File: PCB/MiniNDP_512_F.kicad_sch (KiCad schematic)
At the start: 15 parts, among them J1 Conn_02x20_Odd_Even, U1 HC238, U2 HC4040, U3 FCT841, U4 AS6C4008, U5 2G00

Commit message: 512k F easy build
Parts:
- removed C5: 10u, 000_LOCAL:C_0805, symbol 000_LOCAL:C
- removed D1: BAS70-05, 000_LOCAL:SOT-23, symbol 000_LOCAL:BAV70
- removed R3: 47k, 000_LOCAL:R_0805, symbol 000_LOCAL:R
- added C1: 4.7u, 000_LOCAL:C_1206, symbol 000_LOCAL:C
- added D1, D2: LL4148, 000_LOCAL:D_MiniMELF, symbol 000_LOCAL:LL4148
- added R1: 47k, 000_LOCAL:R_1206, symbol 000_LOCAL:R
- C2: footprint 000_LOCAL:C_0805 -> 000_LOCAL:C_1206; MPN CL21B105KAFNNNE -> CL31B475KAHNNNE
- C3, C4: value 1u -> 4.7u; footprint 000_LOCAL:C_0805 -> 000_LOCAL:C_1206; MPN CL21B105KAFNNNE -> CL31B475KAHNNNE
- R2: footprint 000_LOCAL:R_0805 -> 000_LOCAL:R_1206; MPN RMCF0805FT47K0 -> CRGCQ1206F47K
- U1: MPN (none) -> 74HCT238D,653
- U2: MPN IC BINARY COUNTER 12-BIT 16SO -> 74HC4040D,653
- U3: MPN (none) -> CY74FCT841CTSOC
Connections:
- net +BATT: now also D2.2 (A)
- net GND: now also C1.2
- net RAMRST: now also R1.2; no longer R2.2
- net VBUS: now also C1.1, D1.2 (A); no longer C4.1
- net VMEM: now also C4.1, D1.1 (K), D2.1 (K), R1.1
- net ~{WR}: now also R2.2
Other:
- moved on the sheet: BT1

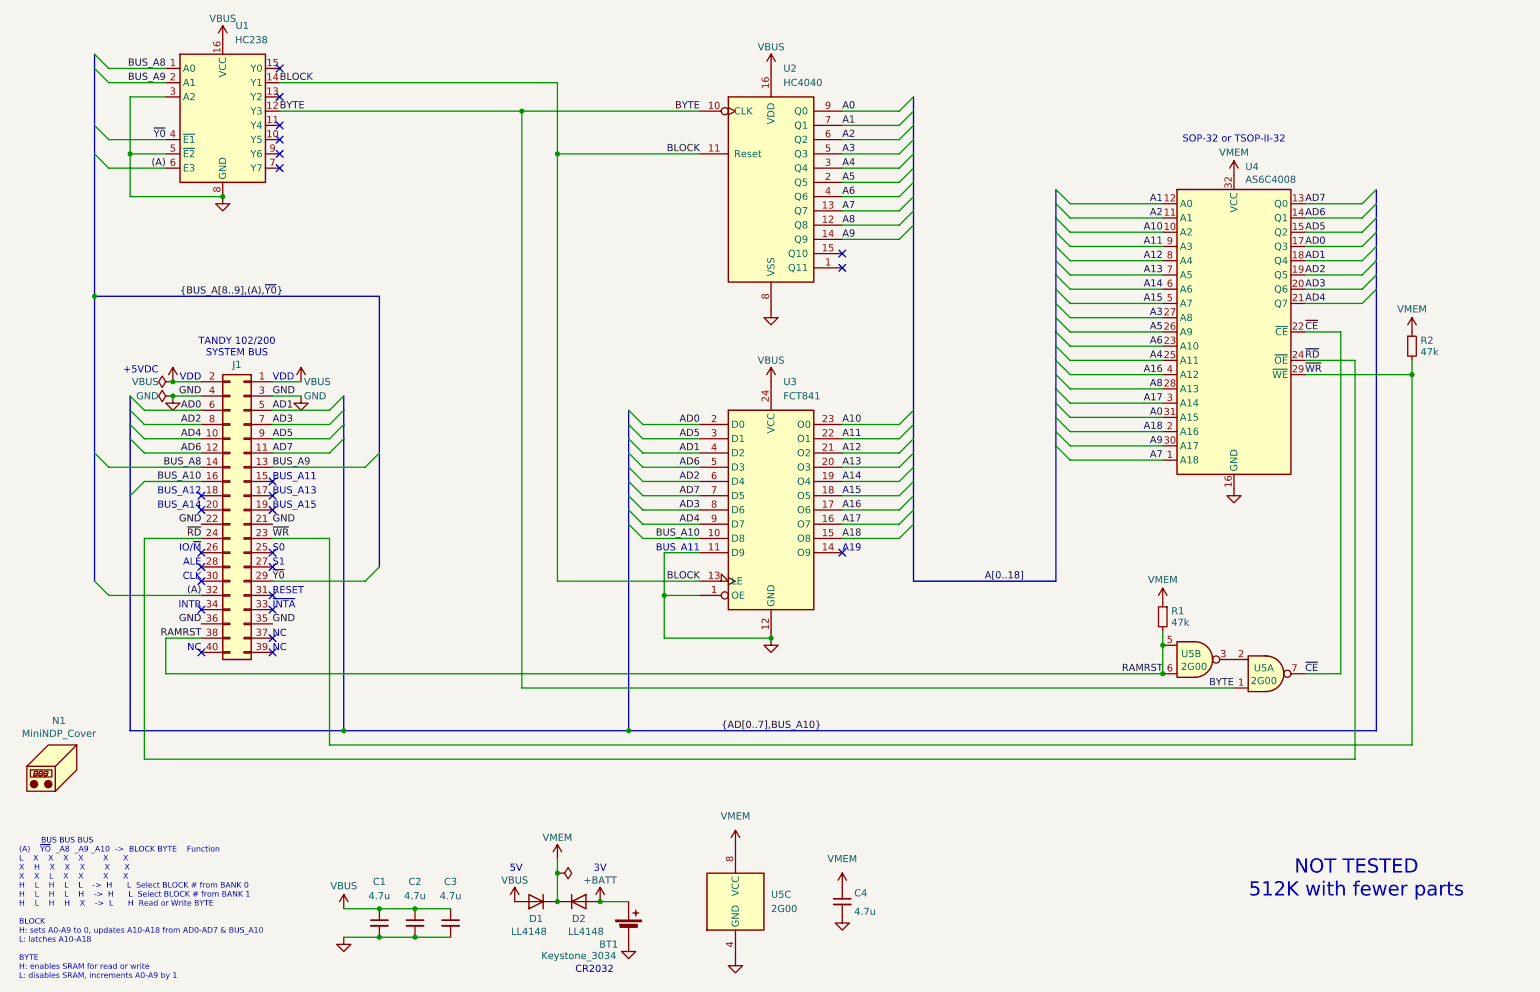
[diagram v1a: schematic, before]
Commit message: replace 512_F with 512_G
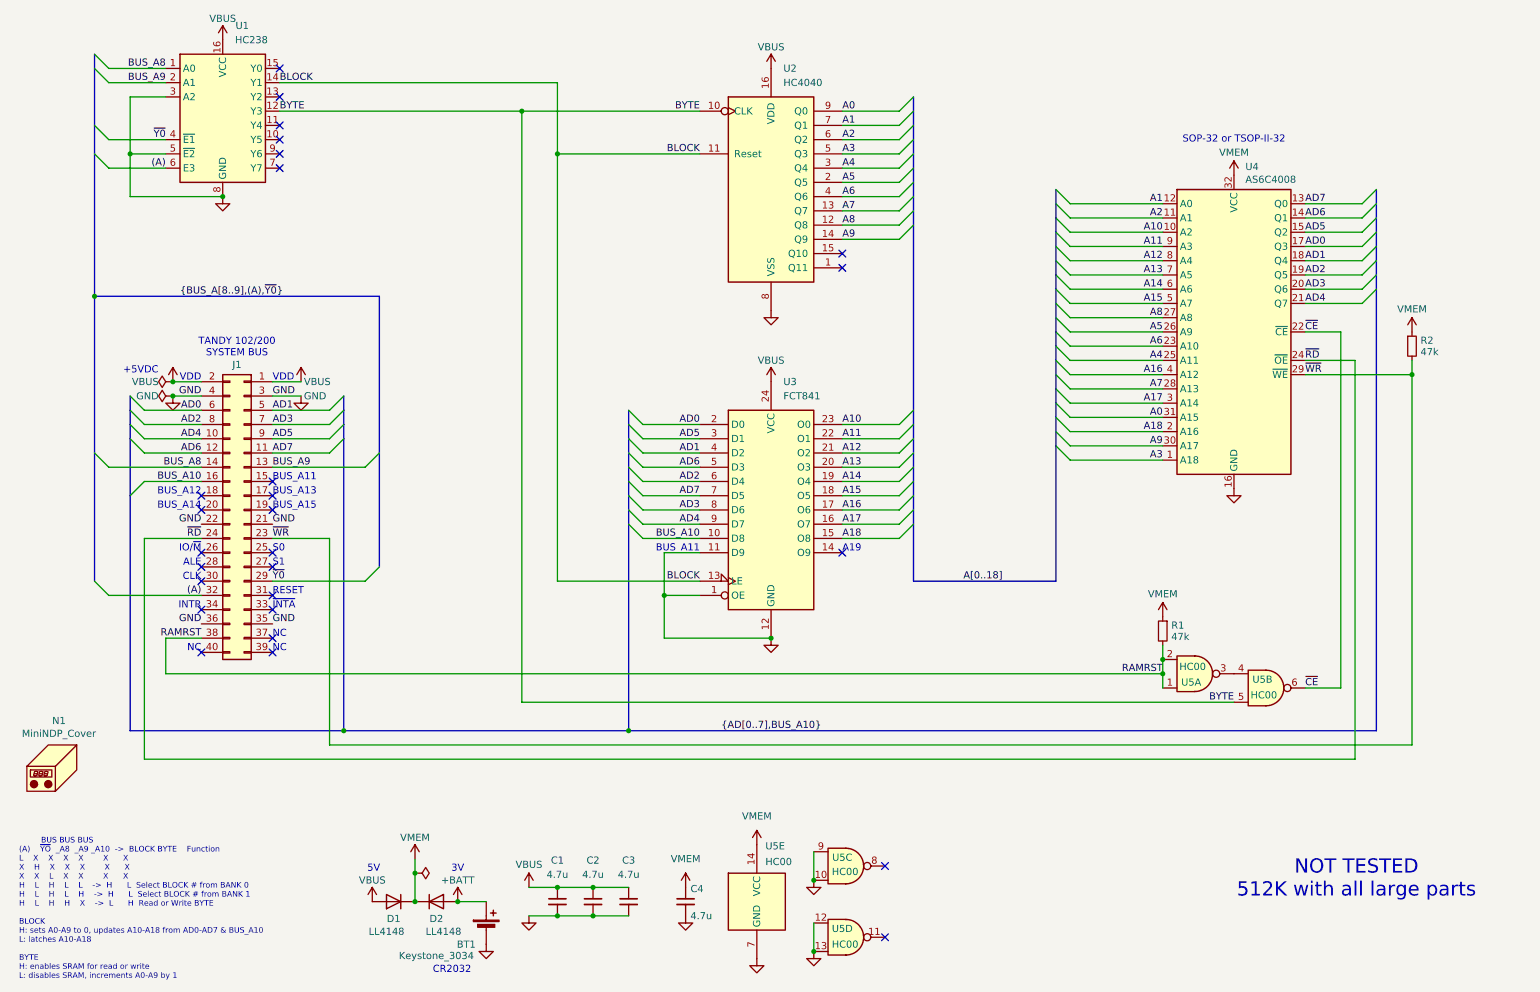
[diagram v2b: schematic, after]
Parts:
- removed U5: 2G00, 000_LOCAL:TSSOP-8_3x3mm_P0.65mm, symbol 000_LOCAL:2G00
- added U5: HC00, 000_LOCAL:SOIC-14_3.9x8.7mm_P1.27mm, symbol 000_LOCAL:74xx00
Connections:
- net A3: now also U4.1 (A18); no longer U4.27 (A8)
- net A7: now also U4.28 (A13); no longer U4.1 (A18)
- net A8: now also U4.27 (A8); no longer U4.28 (A13)
- net BYTE: now also U5.5
- net GND: now also U5.10, U5.12, U5.13, U5.7 (GND), U5.9
- net RAMRST: now also U5.1, U5.2
- net VMEM: now also U5.14 (VCC)
- net ~{CE}: now also U5.6
- new net: U5.3, U5.4
- no-connect marks 25 -> 27
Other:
- note added: "NOT TESTED 512K with all large parts"
- note removed: "NOT TESTED 512K with fewer parts"
- moved on the sheet: BT1, C1, C2, C3, C4, D1, D2, R1

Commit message: 512-F re-add ramrst diode, both-F remove /WR pullup
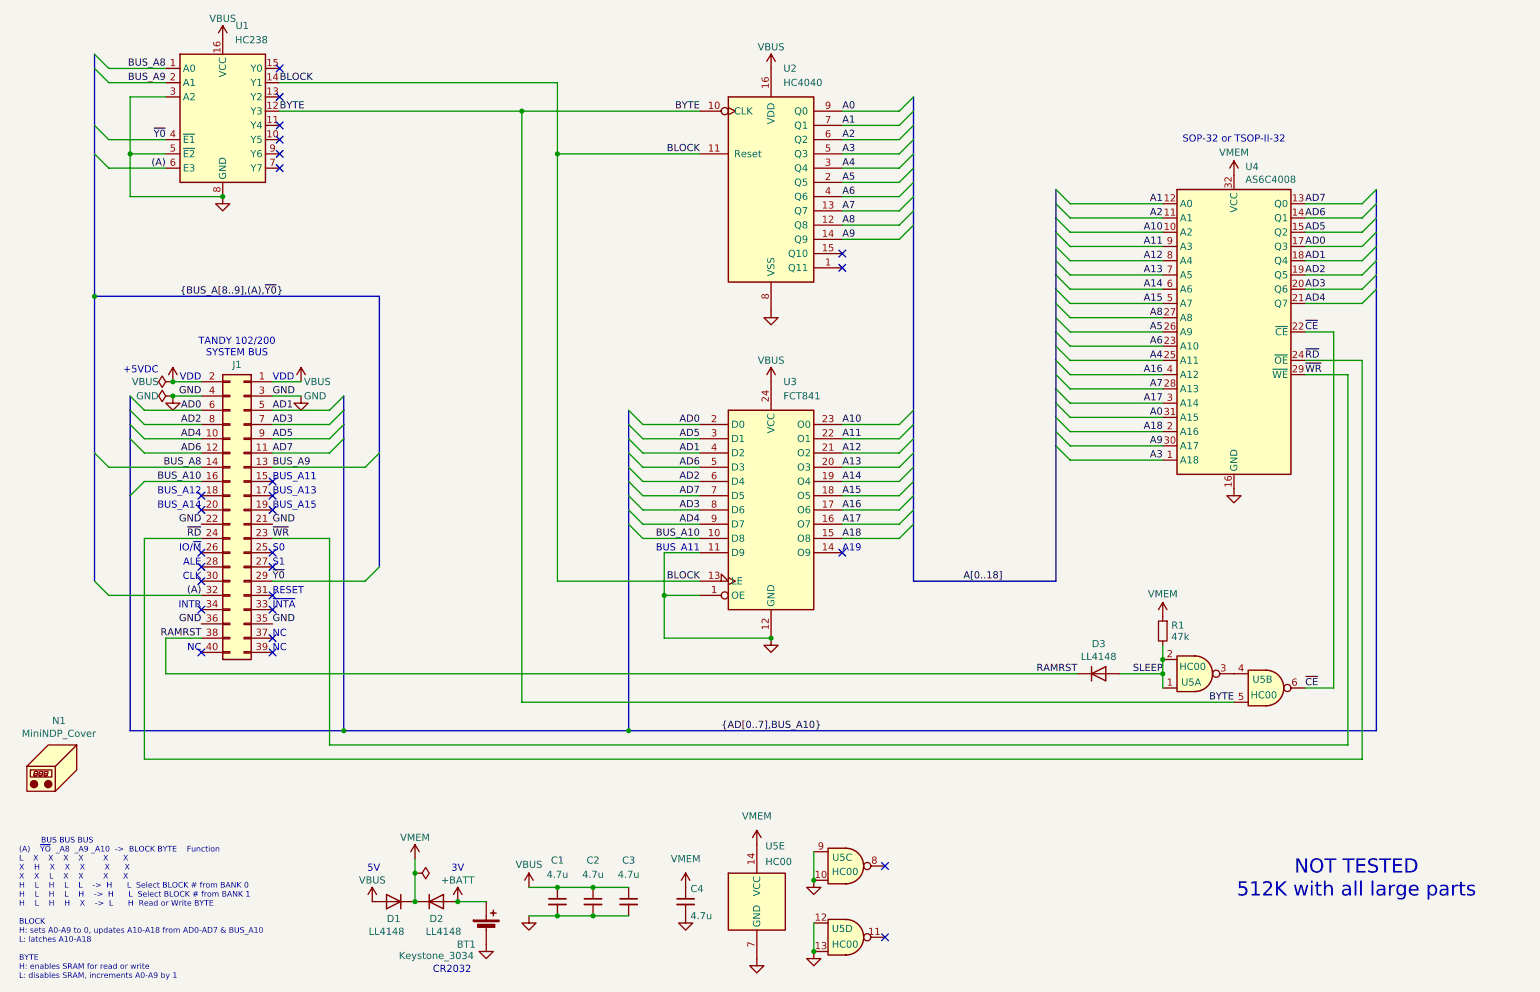
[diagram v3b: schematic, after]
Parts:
- removed R2: 47k, 000_LOCAL:R_1206, symbol 000_LOCAL:R
- added D3: LL4148, 000_LOCAL:D_MiniMELF, symbol 000_LOCAL:LL4148
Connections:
- net RAMRST: now also D3.1 (K); no longer R1.2, U5.1, U5.2
- new net SLEEP: D3.2 (A), R1.2, U5.1, U5.2
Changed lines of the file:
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@@
 		(title "MiniNDP 512")
 		(date "2024-11-26")
-		(rev "F02")
+		(rev "F03")
 		(company "Brian K. White - b.kenyon.w@gmail.com")
 		(comment 1 "github.com/bkw777/NODE_DATAPAC")
@@
 	)
 	(junction
-		(at 266.7 83.82)
-		(diameter 0)
-		(color 0 0 0 0)
-	)
-	(junction
 		(at 222.25 134.62)
 		(diameter 0)
@@
 	(wire
 		(pts
+			(xy 214.63 137.16) (xy 222.25 137.16)
+		)
+		(stroke
+			(width 0)
+			(type default)
+		)
+	)
+	(wire
+		(pts
 			(xy 165.1 41.91) (xy 175.26 41.91)
 		)
@@
 	(wire
 		(pts
-			(xy 247.65 139.7) (xy 254 139.7)
-		)
-		(stroke
-			(width 0)
-			(type default)
-		)
-	)
-	(wire
-		(pts
 			(xy 44.45 130.81) (xy 44.45 137.16)
 		)
@@
 	(wire
 		(pts
+			(xy 255.27 83.82) (xy 255.27 149.86)
+		)
+		(stroke
+			(width 0)
+			(type default)
+		)
+	)
+	(wire
+		(pts
 			(xy 205.74 91.44) (xy 222.25 91.44)
 		)
@@
 	(wire
 		(pts
-			(xy 247.65 83.82) (xy 266.7 83.82)
+			(xy 247.65 83.82) (xy 255.27 83.82)
 		)
 		(stroke
@@
 	(wire
 		(pts
+			(xy 252.73 76.2) (xy 252.73 139.7)
+		)
+		(stroke
+			(width 0)
+			(type default)
+		)
+	)
+	(wire
+		(pts
 			(xy 129.54 97.79) (xy 139.7 97.79)
 		)
@@
 		)
 	)
+	(wire
+		(pts
+			(xy 247.65 139.7) (xy 252.73 139.7)
+		)
+		(stroke
+			(width 0)
+			(type default)
+		)
+	)
 	(bus
 		(pts
@@
 	(wire
 		(pts
-			(xy 266.7 83.82) (xy 266.7 149.86)
-		)
-		(stroke
-			(width 0)
-			(type default)
-		)
-	)
-	(wire
-		(pts
 			(xy 247.65 68.58) (xy 257.81 68.58)
 		)
@@
 	(wire
 		(pts
-			(xy 266.7 81.28) (xy 266.7 83.82)
-		)
-		(stroke
-			(width 0)
-			(type default)
-		)
-	)
-	(wire
-		(pts
 			(xy 50.8 113.03) (xy 40.64 113.03)
 		)
@@
 	(wire
 		(pts
-			(xy 266.7 149.86) (xy 73.66 149.86)
+			(xy 255.27 149.86) (xy 73.66 149.86)
 		)
 		(stroke
@@
 		)
 	)
-	(wire
-		(pts
-			(xy 254 76.2) (xy 254 139.7)
-		)
-		(stroke
-			(width 0)
-			(type default)
-		)
-	)
 	(bus
 		(pts
@@
 	(wire
 		(pts
-			(xy 254 76.2) (xy 247.65 76.2)
+			(xy 88.9 170.18) (xy 88.9 172.72)
 		)
 		(stroke
@@
 		)
 	)
-	(wire
+	(bus
 		(pts
-			(xy 88.9 170.18) (xy 88.9 172.72)
+			(xy 203.2 78.74) (xy 203.2 81.28)
 		)
 		(stroke
@@
 		)
 	)
-	(bus
+	(wire
 		(pts
-			(xy 203.2 78.74) (xy 203.2 81.28)
+			(xy 247.65 81.28) (xy 257.81 81.28)
 		)
 		(stroke
@@
 		)
 	)
-	(wire
+	(bus
 		(pts
-			(xy 247.65 81.28) (xy 256.54 81.28)
+			(xy 203.2 58.42) (xy 203.2 60.96)
 		)
 		(stroke
@@
 		)
 	)
-	(bus
+	(wire
 		(pts
-			(xy 203.2 58.42) (xy 203.2 60.96)
+			(xy 252.73 76.2) (xy 247.65 76.2)
 		)
 		(stroke
@@
 	(wire
 		(pts
-			(xy 256.54 152.4) (xy 256.54 81.28)
+			(xy 257.81 152.4) (xy 257.81 81.28)
 		)
 		(stroke
@@
 	(wire
 		(pts
-			(xy 44.45 137.16) (xy 222.25 137.16)
+			(xy 44.45 137.16) (xy 207.01 137.16)
 		)
 		(stroke
@@
 	(wire
 		(pts
-			(xy 40.64 152.4) (xy 256.54 152.4)
+			(xy 40.64 152.4) (xy 257.81 152.4)
 		)
 		(stroke
@@
 	)
 	(label "RAMRST"
-		(at 222.25 137.16 180)
+		(at 207.01 137.16 180)
 		(fields_autoplaced yes)
 		(effects
@@
 		)
 	)
+	(label "SLEEP"
+		(at 222.25 137.16 180)
+		(fields_autoplaced yes)
+		(effects
+			(font
+				(size 1.27 1.27)
+			)
+			(justify right bottom)
+		)
+	)
 	(label "BUS_A9"
 		(at 63.5 100.33 0)
@@
 	)
 	(symbol
-		(lib_id "000_LOCAL:R")
-		(at 266.7 78.74 0)
-		(unit 1)
-		(exclude_from_sim no)
-		(in_bom yes)
-		(on_board yes)
-		(dnp no)
-		(property "Reference" "R2"
-			(at 268.224 77.724 0)
-			(effects
-				(font
-					(size 1.27 1.27)
-				)
-				(justify left)
-			)
-		)
-		(property "Value" "47k"
-			(at 268.224 79.756 0)
-			(effects
-				(font
-					(size 1.27 1.27)
-				)
-				(justify left)
-			)
-		)
-		(property "Footprint" "000_LOCAL:R_1206"
-			(at 266.7 78.74 0)
-			(effects
-				(font
-					(size 1.27 1.27)
-				)
-				(hide yes)
-			)
-		)
-		(property "Datasheet" "datasheets/TE-4-2176343-5.pdf"
-			(at 266.7 78.74 0)
-			(effects
-				(font
-					(size 1.27 1.27)
-				)
-				(hide yes)
-			)
-		)
-		(property "Description" "RES 47K OHM 1% 1/4W 1206"
-			(at 266.7 78.74 0)
-			(effects
-				(font
-					(size 1.27 1.27)
-				)
-				(hide yes)
-			)
-		)
-		(property "MPN" "CRGCQ1206F47K"
-			(at 266.7 78.74 0)
-			(effects
-				(font
-					(size 1.27 1.27)
-				)
-				(hide yes)
-			)
-		)
-		(pin "1"
-		)
-		(pin "2"
-		)
-		(instances
-			(project "MiniNDP_512_F"
-				(path "/f15c2929-5cf4-4b4e-965d-148e1bec8a42"
-					(reference "R2")
-					(unit 1)
-				)
-			)
-		)
-	)
-	(symbol
 		(lib_id "power:VMEM")
 		(at 88.9 170.18 0)
@@
 	)
 	(symbol
+		(lib_id "000_LOCAL:LL4148")
+		(at 210.82 137.16 0)
+		(unit 1)
+		(exclude_from_sim no)
+		(in_bom yes)
+		(on_board yes)
+		(dnp no)
+		(property "Reference" "D3"
+			(at 210.82 131.826 0)
+			(effects
+				(font
+					(size 1.27 1.27)
+				)
+			)
+		)
+		(property "Value" "LL4148"
+			(at 210.82 134.112 0)
+			(effects
+				(font
+					(size 1.27 1.27)
+				)
+			)
+		)
+		(property "Footprint" "000_LOCAL:D_MiniMELF"
+			(at 210.82 137.16 0)
+			(effects
+				(font
+					(size 1.27 1.27)
+				)
+				(hide yes)
+			)
+		)
+		(property "Datasheet" "datasheets/ll4148.pdf"
+			(at 210.82 137.16 0)
+			(effects
+				(font
+					(size 1.27 1.27)
+				)
+				(hide yes)
+			)
+		)
+		(property "Description" "50V 1A General Purpose Rectifier Diode"
+			(at 210.82 137.16 0)
+			(effects
+				(font
+					(size 1.27 1.27)
+				)
+				(hide yes)
+			)
+		)
+		(property "MPN" "FDLL4148"
+			(at 210.82 137.16 0)
+			(effects
+				(font
+					(size 1.27 1.27)
+				)
+				(hide yes)
+			)
+		)
+		(pin "1"
+		)
+		(pin "2"
+		)
+		(instances
+			(project "MiniNDP_512_F"
+				(path "/f15c2929-5cf4-4b4e-965d-148e1bec8a42"
+					(reference "D3")
+					(unit 1)
+				)
+			)
+		)
+	)
+	(symbol
 		(lib_id "power:GND")
 		(at 45.72 87.63 0)
@@
 					(unit 1)
 				)
-			)
-		)
-	)
-	(symbol
-		(lib_id "power:VMEM")
-		(at 266.7 76.2 0)
-		(unit 1)
-		(exclude_from_sim no)
-		(in_bom yes)
-		(on_board yes)
-		(dnp no)
-		(property "Reference" "#PWR014"
-			(at 266.7 80.01 0)
-			(effects
-				(font
-					(size 1.27 1.27)
-				)
-				(hide yes)
-			)
-		)
-		(property "Value" "VMEM"
-			(at 266.7 72.136 0)
-			(effects
-				(font
-					(size 1.27 1.27)
-				)
-			)
-		)
-		(property "Footprint" ""
-			(at 266.7 76.2 0)
-			(effects
-				(font
-					(size 1.27 1.27)
-				)
-				(hide yes)
-			)
-		)
-		(property "Datasheet" ""
-			(at 266.7 76.2 0)
-			(effects
-				(font
-					(size 1.27 1.27)
-				)
-				(hide yes)
-			)
-		)
-		(property "Description" "Power symbol creates a global label with name \"VMEM\""
-			(at 266.7 76.2 0)
-			(effects
-				(font
-					(size 1.27 1.27)
-				)
-				(hide yes)
-			)
-		)
-		(pin "1"
-		)
-		(instances
-			(project "MiniNDP_512_B"
-				(path "/f15c2929-5cf4-4b4e-965d-148e1bec8a42"
-					(reference "#PWR014")
-					(unit 1)
-				)

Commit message: 512_F 1M_C remove ramrst diode, 1u caps
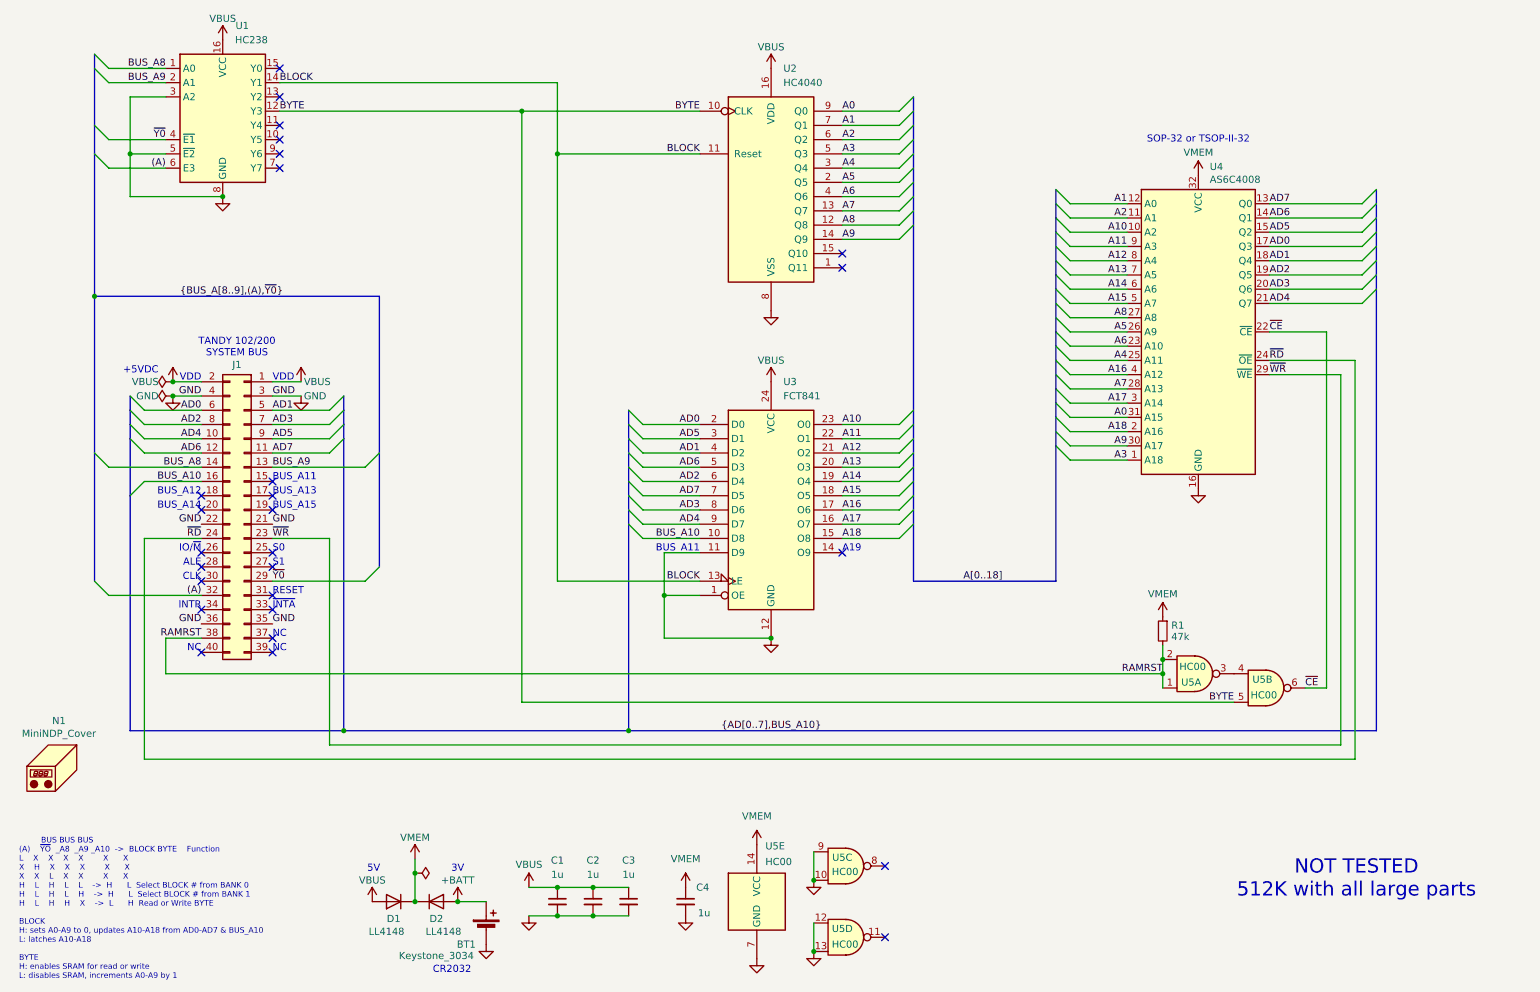
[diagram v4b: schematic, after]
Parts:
- removed D3: LL4148, 000_LOCAL:D_MiniMELF, symbol 000_LOCAL:LL4148
- C1, C2, C3, C4: value 4.7u -> 1u; MPN CL31B475KAHNNNE -> CL31B105KAHNNNE
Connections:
- net SLEEP is gone; now on net RAMRST: R1.2, U5.1, U5.2
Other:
- moved on the sheet: U4
